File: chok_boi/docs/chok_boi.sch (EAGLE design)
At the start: 94 parts, among them IC1 L293DD, U1 MPU-6000

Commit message: Finish component placement. Start routing
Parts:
- renumbered C_5V10 to C_GY_VDD, C_5V11 to C_GY_REG, C_5V12 to C_GY_CP, R_ERF_PD1 to R_EH_PD, R_ES_PD to R_ED_PD
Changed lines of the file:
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@@
 <part name="U$11" library="sfh4550 _ teft4300" deviceset="EMITTER" device=""/>
 <part name="R_ED1" library="SparkFun-Passives" deviceset="RESISTOR" device="0603-RES" value="5.6"/>
-<part name="R_ES_PD" library="SparkFun-Passives" deviceset="RESISTOR" device="0603-RES" value="47k"/>
+<part name="R_ED_PD" library="SparkFun-Passives" deviceset="RESISTOR" device="0603-RES" value="47k"/>
 <part name="U$13" library="sfh4550 _ teft4300" deviceset="EMITTER" device=""/>
 <part name="R_ERF" library="SparkFun-Passives" deviceset="RESISTOR" device="0603-RES" value="10"/>
@@
 <part name="R_EH1" library="SparkFun-Passives" deviceset="RESISTOR" device="0603-RES" value="5.6"/>
 <part name="R_EH2" library="SparkFun-Passives" deviceset="RESISTOR" device="0603-RES" value="5.6"/>
-<part name="R_ERF_PD1" library="SparkFun-Passives" deviceset="RESISTOR" device="0603-RES" value="47k"/>
+<part name="R_EH_PD" library="SparkFun-Passives" deviceset="RESISTOR" device="0603-RES" value="47k"/>
 <part name="C_E_H2" library="SparkFun-Capacitors" deviceset="CAP" device="0603-CAP" value="0.1uF"/>
 <part name="C_E_H1" library="SparkFun-Capacitors" deviceset="CAP" device="0603-CAP" value="4.7uF"/>
@@
 <part name="C_REC_LH" library="SparkFun" deviceset="CAP" device="0603-CAP" value="0.1uF"/>
 <part name="C_REC_LF" library="SparkFun" deviceset="CAP" device="0603-CAP" value="0.1uF"/>
-<part name="C_5V11" library="SparkFun" deviceset="CAP" device="0603-CAP" value="0.1uF"/>
-<part name="C_5V12" library="SparkFun" deviceset="CAP" device="0603-CAP" value="2.2nF"/>
-<part name="C_5V10" library="SparkFun" deviceset="CAP" device="0603-CAP" value="0.01uF"/>
+<part name="C_GY_REG" library="SparkFun" deviceset="CAP" device="0603-CAP" value="0.1uF"/>
+<part name="C_GY_CP" library="SparkFun" deviceset="CAP" device="0603-CAP" value="2.2nF"/>
+<part name="C_GY_VDD" library="SparkFun" deviceset="CAP" device="0603-CAP" value="0.01uF"/>
 <part name="AGND5" library="supply1" library_urn="urn:adsk.eagle:library:371" deviceset="AGND" device=""/>
 <part name="T1" library="zetex" library_urn="urn:adsk.eagle:library:418" deviceset="NPNSOT323" device="" package3d_urn="urn:adsk.eagle:package:30986/1"/>
@@
 <instance part="U$11" gate="G$1" x="218.44" y="-20.32"/>
 <instance part="R_ED1" gate="G$1" x="218.44" y="-50.8" rot="R90"/>
-<instance part="R_ES_PD" gate="G$1" x="200.66" y="-73.66" rot="R90"/>
+<instance part="R_ED_PD" gate="G$1" x="200.66" y="-73.66" rot="R90"/>
 <instance part="U$13" gate="G$1" x="284.48" y="-27.94"/>
 <instance part="R_ERF" gate="G$1" x="284.48" y="-45.72" rot="R90"/>
@@
 <instance part="R_EH1" gate="G$1" x="335.28" y="-50.8" rot="R90"/>
 <instance part="R_EH2" gate="G$1" x="345.44" y="-50.8" rot="R90"/>
-<instance part="R_ERF_PD1" gate="G$1" x="322.58" y="-71.12" rot="R90"/>
+<instance part="R_EH_PD" gate="G$1" x="322.58" y="-71.12" rot="R90"/>
 <instance part="C_E_H2" gate="G$1" x="363.22" y="-30.48"/>
 <instance part="C_E_H1" gate="G$1" x="353.06" y="-30.48"/>
@@
 <instance part="C_REC_LH" gate="G$1" x="358.14" y="58.42"/>
 <instance part="C_REC_LF" gate="G$1" x="170.18" y="58.42"/>
-<instance part="C_5V11" gate="G$1" x="22.86" y="-93.98"/>
-<instance part="C_5V12" gate="G$1" x="35.56" y="-93.98"/>
-<instance part="C_5V10" gate="G$1" x="15.24" y="-71.12"/>
+<instance part="C_GY_REG" gate="G$1" x="22.86" y="-93.98"/>
+<instance part="C_GY_CP" gate="G$1" x="35.56" y="-93.98"/>
+<instance part="C_GY_VDD" gate="G$1" x="15.24" y="-71.12"/>
 <instance part="AGND5" gate="VR1" x="22.86" y="-101.6"/>
 <instance part="T1" gate="A" x="160.02" y="-66.04"/>
@@
 <wire x1="162.56" y1="-81.28" x2="144.78" y2="-81.28" width="0.1524" layer="91"/>
 <wire x1="144.78" y1="-81.28" x2="144.78" y2="-78.74" width="0.1524" layer="91"/>
-<pinref part="R_ES_PD" gate="G$1" pin="1"/>
+<pinref part="R_ED_PD" gate="G$1" pin="1"/>
 <wire x1="233.68" y1="-81.28" x2="218.44" y2="-81.28" width="0.1524" layer="91"/>
 <wire x1="218.44" y1="-81.28" x2="200.66" y2="-81.28" width="0.1524" layer="91"/>
@@
 <wire x1="353.06" y1="-81.28" x2="335.28" y2="-81.28" width="0.1524" layer="91"/>
 <junction x="353.06" y="-33.02"/>
-<pinref part="R_ERF_PD1" gate="G$1" pin="1"/>
+<pinref part="R_EH_PD" gate="G$1" pin="1"/>
 <wire x1="335.28" y1="-81.28" x2="322.58" y2="-81.28" width="0.1524" layer="91"/>
 <wire x1="322.58" y1="-76.2" x2="322.58" y2="-81.28" width="0.1524" layer="91"/>
@@
 </segment>
 <segment>
-<pinref part="C_5V10" gate="G$1" pin="2"/>
+<pinref part="C_GY_VDD" gate="G$1" pin="2"/>
 <wire x1="15.24" y1="-73.66" x2="15.24" y2="-99.06" width="0.1524" layer="91"/>
 <wire x1="15.24" y1="-99.06" x2="22.86" y2="-99.06" width="0.1524" layer="91"/>
-<pinref part="C_5V11" gate="G$1" pin="2"/>
+<pinref part="C_GY_REG" gate="G$1" pin="2"/>
 <wire x1="22.86" y1="-96.52" x2="22.86" y2="-99.06" width="0.1524" layer="91"/>
 <junction x="22.86" y="-99.06"/>
-<pinref part="C_5V12" gate="G$1" pin="2"/>
+<pinref part="C_GY_CP" gate="G$1" pin="2"/>
 <wire x1="35.56" y1="-96.52" x2="35.56" y2="-99.06" width="0.1524" layer="91"/>
 <wire x1="35.56" y1="-99.06" x2="22.86" y2="-99.06" width="0.1524" layer="91"/>
@@
 <wire x1="43.18" y1="-71.12" x2="45.72" y2="-71.12" width="0.1524" layer="91"/>
 <label x="7.62" y="-63.5" size="1.778" layer="95" rot="R180" xref="yes"/>
-<pinref part="C_5V10" gate="G$1" pin="1"/>
+<pinref part="C_GY_VDD" gate="G$1" pin="1"/>
 <wire x1="15.24" y1="-66.04" x2="15.24" y2="-63.5" width="0.1524" layer="91"/>
 <junction x="15.24" y="-63.5"/>
@@
 <net name="EM_D" class="0">
 <segment>
-<pinref part="R_ES_PD" gate="G$1" pin="2"/>
+<pinref part="R_ED_PD" gate="G$1" pin="2"/>
 <wire x1="200.66" y1="-68.58" x2="200.66" y2="-66.04" width="0.1524" layer="91"/>
 <label x="200.66" y="-53.34" size="1.778" layer="95" rot="R180" xref="yes"/>
@@
 <net name="EM_H" class="0">
 <segment>
-<pinref part="R_ERF_PD1" gate="G$1" pin="2"/>
+<pinref part="R_EH_PD" gate="G$1" pin="2"/>
 <wire x1="322.58" y1="-66.04" x2="322.58" y2="-63.5" width="0.1524" layer="91"/>
 <label x="322.58" y="-55.88" size="1.778" layer="95" rot="R180" xref="yes"/>
@@
 <net name="N$20" class="0">
 <segment>
-<pinref part="C_5V11" gate="G$1" pin="1"/>
+<pinref part="C_GY_REG" gate="G$1" pin="1"/>
 <wire x1="22.86" y1="-88.9" x2="22.86" y2="-81.28" width="0.1524" layer="91"/>
 <pinref part="U1" gate="G$1" pin="REGOUT"/>
@@
 <net name="N$22" class="0">
 <segment>
-<pinref part="C_5V12" gate="G$1" pin="1"/>
+<pinref part="C_GY_CP" gate="G$1" pin="1"/>
 <pinref part="U1" gate="G$1" pin="CPOUT"/>
 <wire x1="35.56" y1="-88.9" x2="35.56" y2="-83.82" width="0.1524" layer="91"/>

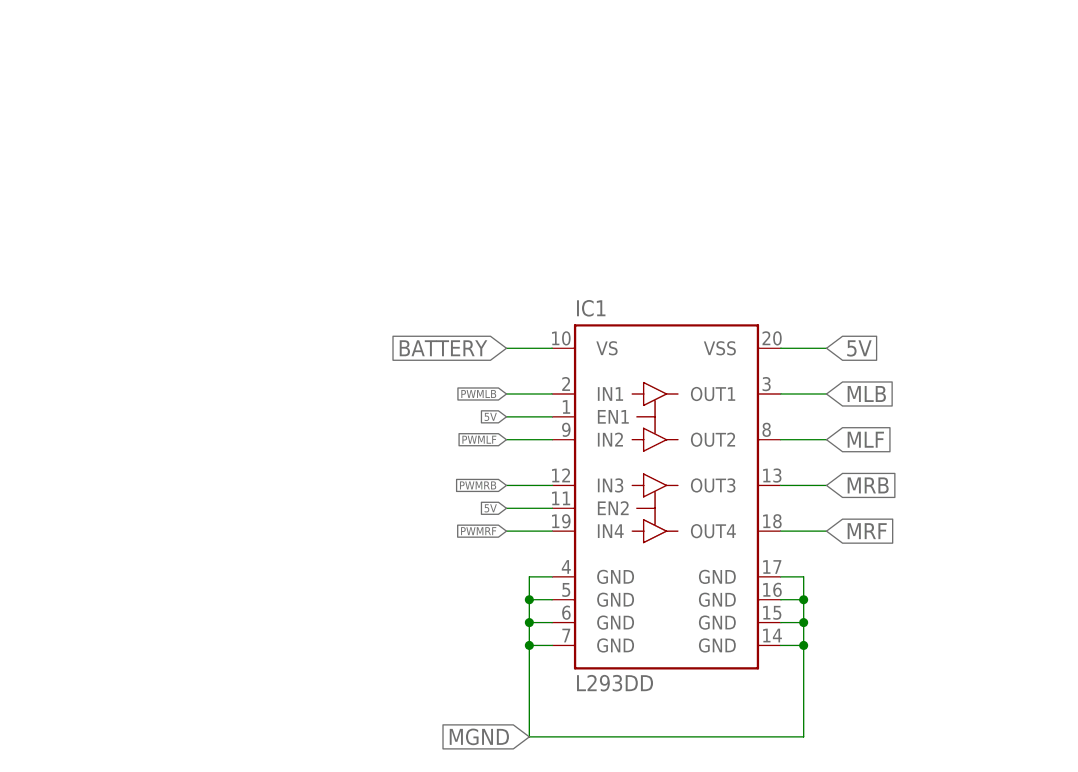
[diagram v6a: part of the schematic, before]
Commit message: Add DRV8835 motor driver
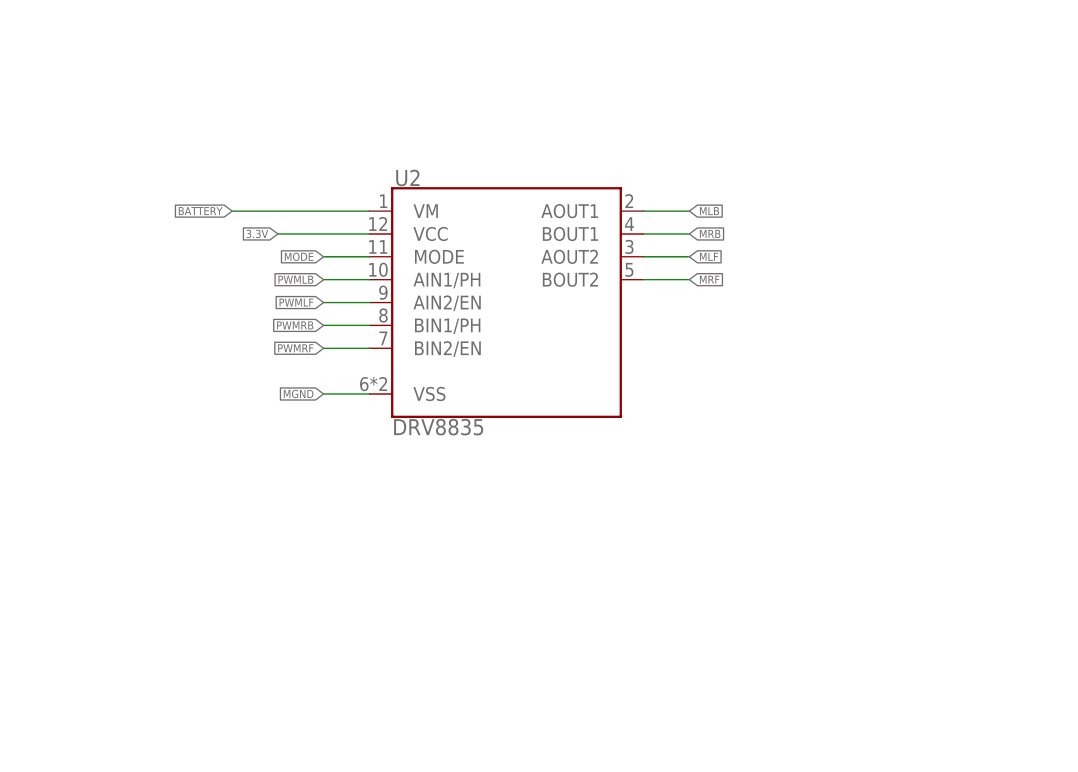
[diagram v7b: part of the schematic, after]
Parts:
- removed IC1: L293DD, st-microelectronics:L293DD
- added U2: DRV8835, SparkFun-IC-Special-Function:DRV883X
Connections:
- new net MODE: U2.MODE
- net 3.3V: now also U2.VCC
- net 5V: no longer IC1.EN1, IC1.EN2, IC1.VSS
- net BATTERY: now also U2.VM; no longer IC1.VS
- net MGND: now also U2.VSS; no longer IC1.GND@1, IC1.GND@2, IC1.GND@3, IC1.GND@4, IC1.GND@5, IC1.GND@6, IC1.GND@7, IC1.GND@8
- net MLB: now also U2.AOUT1; no longer IC1.OUT1
- net MLF: now also U2.AOUT2; no longer IC1.OUT2
- net MRB: now also U2.BOUT1; no longer IC1.OUT3
- net MRF: now also U2.BOUT2; no longer IC1.OUT4
- net PWMLB: now also U2.AIN1/PH; no longer IC1.IN1
- net PWMLF: now also U2.AIN2/EN; no longer IC1.IN2
- net PWMRB: now also U2.BIN1/PH; no longer IC1.IN3
- net PWMRF: now also U2.BIN2/EN; no longer IC1.IN4

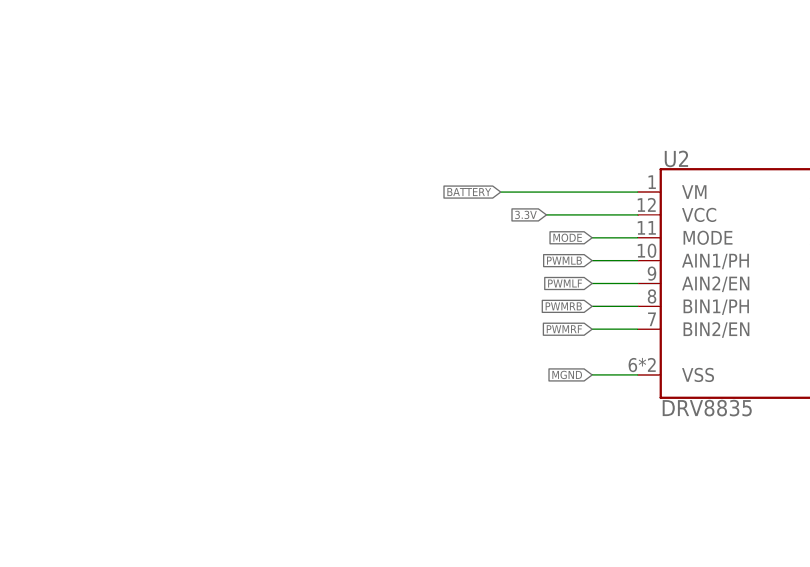
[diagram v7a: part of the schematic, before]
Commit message: Add bypass caps to DRV8835
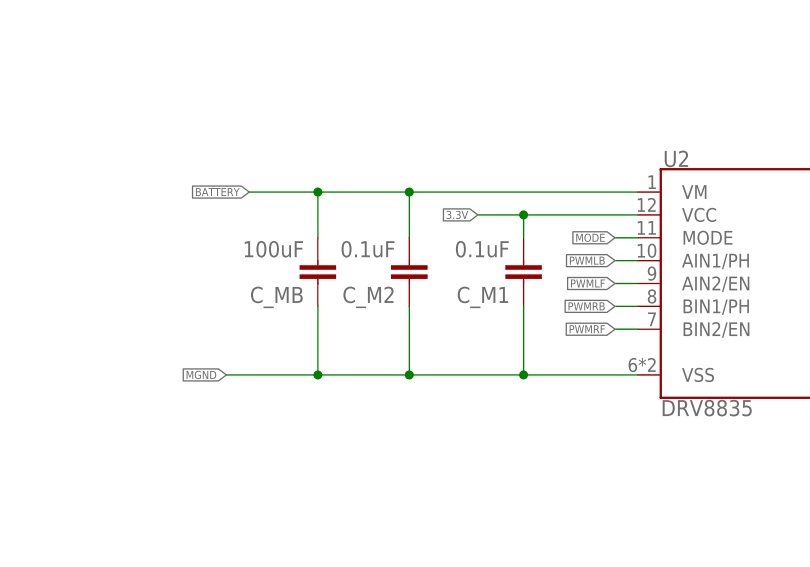
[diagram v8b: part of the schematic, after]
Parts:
- added C_M1, C_M2: 0.1uF, SparkFun:CAP0603-CAP
- added C_MB: 100uF, SparkFun:CAP0603-CAP
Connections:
- net 3.3V: now also C_M1.2
- net BATTERY: now also C_M2.2, C_MB.2
- net MGND: now also C_M1.1, C_M2.1, C_MB.1
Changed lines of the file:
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@@
 <part name="AGND6" library="supply1" library_urn="urn:adsk.eagle:library:371" deviceset="AGND" device=""/>
 <part name="U2" library="SparkFun-IC-Special-Function" deviceset="DRV883X" device="" value="DRV8835"/>
+<part name="C_M1" library="SparkFun" deviceset="CAP" device="0603-CAP" value="0.1uF"/>
+<part name="C_M2" library="SparkFun" deviceset="CAP" device="0603-CAP" value="0.1uF"/>
+<part name="C_MB" library="SparkFun" deviceset="CAP" device="0603-CAP" value="100uF"/>
 </parts>
 <sheets>
@@
 <instance part="AGND6" gate="VR1" x="27.94" y="-78.74" rot="R270"/>
 <instance part="U2" gate="G$1" x="-137.16" y="-180.34"/>
+<instance part="C_M1" gate="G$1" x="-165.1" y="-177.8" rot="R180"/>
+<instance part="C_M2" gate="G$1" x="-177.8" y="-177.8" rot="R180"/>
+<instance part="C_MB" gate="G$1" x="-187.96" y="-177.8" rot="R180"/>
 </instances>
 <busses>
@@
 <segment>
 <pinref part="U2" gate="G$1" pin="VM"/>
-<wire x1="-152.4" y1="-170.18" x2="-167.64" y2="-170.18" width="0.1524" layer="91"/>
-<label x="-167.64" y="-170.18" size="0.889" layer="95" rot="R180" xref="yes"/>
+<wire x1="-152.4" y1="-170.18" x2="-177.8" y2="-170.18" width="0.1524" layer="91"/>
+<label x="-195.58" y="-170.18" size="0.889" layer="95" rot="R180" xref="yes"/>
+<pinref part="C_M2" gate="G$1" pin="2"/>
+<wire x1="-177.8" y1="-170.18" x2="-187.96" y2="-170.18" width="0.1524" layer="91"/>
+<wire x1="-187.96" y1="-170.18" x2="-195.58" y2="-170.18" width="0.1524" layer="91"/>
+<wire x1="-177.8" y1="-175.26" x2="-177.8" y2="-170.18" width="0.1524" layer="91"/>
+<junction x="-177.8" y="-170.18"/>
+<pinref part="C_MB" gate="G$1" pin="2"/>
+<wire x1="-187.96" y1="-175.26" x2="-187.96" y2="-170.18" width="0.1524" layer="91"/>
+<junction x="-187.96" y="-170.18"/>
 </segment>
 </net>
@@
 <segment>
 <pinref part="U2" gate="G$1" pin="VCC"/>
-<wire x1="-152.4" y1="-172.72" x2="-162.56" y2="-172.72" width="0.1524" layer="91"/>
-<label x="-162.56" y="-172.72" size="0.889" layer="95" rot="R180" xref="yes"/>
+<wire x1="-152.4" y1="-172.72" x2="-165.1" y2="-172.72" width="0.1524" layer="91"/>
+<label x="-170.18" y="-172.72" size="0.889" layer="95" rot="R180" xref="yes"/>
+<pinref part="C_M1" gate="G$1" pin="2"/>
+<wire x1="-165.1" y1="-172.72" x2="-170.18" y2="-172.72" width="0.1524" layer="91"/>
+<wire x1="-165.1" y1="-175.26" x2="-165.1" y2="-172.72" width="0.1524" layer="91"/>
+<junction x="-165.1" y="-172.72"/>
 </segment>
 </net>
@@
 <segment>
 <pinref part="U2" gate="G$1" pin="AIN1/PH"/>
-<wire x1="-152.4" y1="-177.8" x2="-157.48" y2="-177.8" width="0.1524" layer="91"/>
-<label x="-157.48" y="-177.8" size="0.889" layer="95" rot="R180" xref="yes"/>
+<wire x1="-152.4" y1="-177.8" x2="-154.94" y2="-177.8" width="0.1524" layer="91"/>
+<label x="-154.94" y="-177.8" size="0.889" layer="95" rot="R180" xref="yes"/>
 </segment>
 </net>
@@
 <segment>
 <pinref part="U2" gate="G$1" pin="AIN2/EN"/>
-<wire x1="-152.4" y1="-180.34" x2="-157.48" y2="-180.34" width="0.1524" layer="91"/>
-<label x="-157.48" y="-180.34" size="0.889" layer="95" rot="R180" xref="yes"/>
+<wire x1="-152.4" y1="-180.34" x2="-154.94" y2="-180.34" width="0.1524" layer="91"/>
+<label x="-154.94" y="-180.34" size="0.889" layer="95" rot="R180" xref="yes"/>
 </segment>
 </net>
@@
 <segment>
 <pinref part="U2" gate="G$1" pin="BIN1/PH"/>
-<wire x1="-152.4" y1="-182.88" x2="-157.48" y2="-182.88" width="0.1524" layer="91"/>
-<label x="-157.48" y="-182.88" size="0.889" layer="95" rot="R180" xref="yes"/>
+<wire x1="-152.4" y1="-182.88" x2="-154.94" y2="-182.88" width="0.1524" layer="91"/>
+<label x="-154.94" y="-182.88" size="0.889" layer="95" rot="R180" xref="yes"/>
 </segment>
 </net>
@@
 <segment>
 <pinref part="U2" gate="G$1" pin="BIN2/EN"/>
-<wire x1="-152.4" y1="-185.42" x2="-157.48" y2="-185.42" width="0.1524" layer="91"/>
-<label x="-157.48" y="-185.42" size="0.889" layer="95" rot="R180" xref="yes"/>
+<wire x1="-152.4" y1="-185.42" x2="-154.94" y2="-185.42" width="0.1524" layer="91"/>
+<label x="-154.94" y="-185.42" size="0.889" layer="95" rot="R180" xref="yes"/>
 </segment>
 </net>
@@
 <segment>
 <pinref part="U2" gate="G$1" pin="VSS"/>
-<wire x1="-152.4" y1="-190.5" x2="-157.48" y2="-190.5" width="0.1524" layer="91"/>
-<label x="-157.48" y="-190.5" size="0.889" layer="95" rot="R180" xref="yes"/>
+<wire x1="-152.4" y1="-190.5" x2="-165.1" y2="-190.5" width="0.1524" layer="91"/>
+<label x="-198.12" y="-190.5" size="0.889" layer="95" rot="R180" xref="yes"/>
+<pinref part="C_M1" gate="G$1" pin="1"/>
+<wire x1="-165.1" y1="-190.5" x2="-177.8" y2="-190.5" width="0.1524" layer="91"/>
+<wire x1="-177.8" y1="-190.5" x2="-187.96" y2="-190.5" width="0.1524" layer="91"/>
+<wire x1="-187.96" y1="-190.5" x2="-198.12" y2="-190.5" width="0.1524" layer="91"/>
+<wire x1="-165.1" y1="-182.88" x2="-165.1" y2="-190.5" width="0.1524" layer="91"/>
+<junction x="-165.1" y="-190.5"/>
+<pinref part="C_M2" gate="G$1" pin="1"/>
+<wire x1="-177.8" y1="-182.88" x2="-177.8" y2="-190.5" width="0.1524" layer="91"/>
+<junction x="-177.8" y="-190.5"/>
+<pinref part="C_MB" gate="G$1" pin="1"/>
+<wire x1="-187.96" y1="-182.88" x2="-187.96" y2="-190.5" width="0.1524" layer="91"/>
+<junction x="-187.96" y="-190.5"/>
 </segment>
 </net>
@@
 <segment>
 <pinref part="U2" gate="G$1" pin="MODE"/>
-<wire x1="-152.4" y1="-175.26" x2="-157.48" y2="-175.26" width="0.1524" layer="91"/>
-<label x="-157.48" y="-175.26" size="0.889" layer="95" rot="R180" xref="yes"/>
-</segment>
-</net>
+<wire x1="-152.4" y1="-175.26" x2="-154.94" y2="-175.26" width="0.1524" layer="91"/>
+<label x="-154.94" y="-175.26" size="0.889" layer="95" rot="R180" xref="yes"/>
+</segment>
+</net>
